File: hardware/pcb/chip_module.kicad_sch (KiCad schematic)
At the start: 200 parts, among them J12 BTB_DAUGHTER

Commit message: pcb: Ironwood SBT socket + per-datasheet pin fixes + no_connect markers
Step 0 — Ironwood SBT open-top spring-pin socket (emitter face, main board):
  - socket_footprint(): 65 solder pads (64 EM + EM_ANODE) on F.Cu+F.Paste+F.Mask
    at the 0.30mm die-contact pitch, 4 NPTH M2 mount holes, 25x25mm body +
    courtyard. lib_id "qssc:Ironwood_SBT" + symbol; Uchip swapped from
    QSSC_Chip_EM. This is the commercial made-to-order socket that fits the
    20x20mm / 0.30mm-pitch die (no off-the-shelf socket exists at that pitch).
  - Head-board QSSC_Chip_DET (detector face) unchanged: ACF/pogo on B.Cu.

Step 1 — per-datasheet pin audit + (no_connect) emission (addresses
"practically nothing connected per its datasheet"):
  - FT232RL: net pin 24 -> +3V3 (VCC) and pin 23 -> GND (AGND) -- both required
    supply/ground pads per SSOP-28 that were previously unnetted.
  - ADF4351: REFIN- (pin 19) decoupled to GND via new C37 100nF (single-ended
    CMOS ref, datasheet Fig.51); unused RFOUTB+/- (13,14), RFOUTA- (15), SW (5),
    CE (25) declared no_connect per datasheet (unused RF outputs float).
  - add() now takes nc_pins=...; emit_schematic() emits (no_connect) sexps at
    every documented-unused pin: FT232 modem/crystal/LED (12 pins), ADF4351 (5),
    AD7616 parallel-DB bus + SDI/SDOB in 1-wire HW mode (10/chip x4 = 40 head),
    TLC5947 chip2 OUT16-23 + SOUT (9 main).

Both boards: DRC 0/0/0, ERC 0 errors / 0 warnings. 9 PCB tests green.

Co-Authored-By: Claude Code <noreply@anthropic.com>
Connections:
- no-connect marks 0 -> 40
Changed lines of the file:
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@@
 		)
+	)
+	(no_connect
+		(at 753.4 188.89)
+	)
+	(no_connect
+		(at 753.4 190.16)
+	)
+	(no_connect
+		(at 753.4 191.43)
+	)
+	(no_connect
+		(at 753.4 192.7)
+	)
+	(no_connect
+		(at 753.4 193.97)
+	)
+	(no_connect
+		(at 753.4 195.24)
+	)
+	(no_connect
+		(at 753.4 196.51)
+	)
+	(no_connect
+		(at 753.4 197.78)
+	)
+	(no_connect
+		(at 753.4 169.84)
+	)
+	(no_connect
+		(at 753.4 168.57)
+	)
+	(no_connect
+		(at 511.4 208.89)
+	)
+	(no_connect
+		(at 511.4 210.16)
+	)
+	(no_connect
+		(at 511.4 211.43)
+	)
+	(no_connect
+		(at 511.4 212.7)
+	)
+	(no_connect
+		(at 511.4 213.97)
+	)
+	(no_connect
+		(at 511.4 215.24)
+	)
+	(no_connect
+		(at 511.4 216.51)
+	)
+	(no_connect
+		(at 511.4 217.78)
+	)
+	(no_connect
+		(at 511.4 189.84)
+	)
+	(no_connect
+		(at 511.4 188.57)
+	)
+	(no_connect
+		(at 687.4 208.89)
+	)
+	(no_connect
+		(at 687.4 210.16)
+	)
+	(no_connect
+		(at 687.4 211.43)
+	)
+	(no_connect
+		(at 687.4 212.7)
+	)
+	(no_connect
+		(at 687.4 213.97)
+	)
+	(no_connect
+		(at 687.4 215.24)
+	)
+	(no_connect
+		(at 687.4 216.51)
+	)
+	(no_connect
+		(at 687.4 217.78)
+	)
+	(no_connect
+		(at 687.4 189.84)
+	)
+	(no_connect
+		(at 687.4 188.57)
+	)
+	(no_connect
+		(at 445.4 228.89)
+	)
+	(no_connect
+		(at 445.4 230.16)
+	)
+	(no_connect
+		(at 445.4 231.43)
+	)
+	(no_connect
+		(at 445.4 232.7)
+	)
+	(no_connect
+		(at 445.4 233.97)
+	)
+	(no_connect
+		(at 445.4 235.24)
+	)
+	(no_connect
+		(at 445.4 236.51)
+	)
+	(no_connect
+		(at 445.4 237.78)
+	)
+	(no_connect
+		(at 445.4 209.84)
+	)
+	(no_connect
+		(at 445.4 208.57)
 	)
 	(sheet_instances

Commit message: pcb: verify netlist complete per datasheets, fix C_in/C37 placement short
Connection audit (tools/audit_connections.py) confirms both boards are
netlist-complete and datasheet-correct BEFORE routing:

  - ERC: 0 errors both boards (qssc + chip_module). The 145/203 remaining
    messages are all endpoint_off_grid warnings (authored symbols on a
    non-1.27 mm pin grid) -- cosmetic noise.
  - DRC: 0 violations, 0 unconnected pads, 0 footprint errors both boards.
  - Chip die: 64 emitter_cat -> TLC5947 OUT sinks + EM_ANODE -> +12V_EMIT
    on the main board; 64 DET_IN -> TLV9004 TIA -> AD7616 + DET_REF on the
    head. Every chip net has an off-chip destination (audit confirms).
  - All 268 main-board + head "unnetted" IC pins are intentional spares,
    not missing connections: FPGA 185 spare IO balls (99 power balls all
    netted), AD7616 parallel-DB bus + SDI/SDOB in 1-wire HW serial mode,
    FT232 modem/CBUS pins (USB-only; pin 23 AGND + 24 VCC ARE netted),
    ADF4351 NC pins 5/13/14/15/25 per datasheet, TLC5947 chip2 unused
    OUT16-23 + SOUT, and numberless EP/mount-hole cosmetic pads.

Fix: the main board had 3 DRC violations (shorting_items +5V_IN/ADF_TEMP,
courtyards_overlap, solder_mask_bridge) all from ONE root cause -- the new
input-bulk cap C_in and the ADF4351 TEMP decoupler C37 both fell through
assign_pcb_positions()'s else-branch to the (50,50) default cell, so
C_in.1 (+5V_IN) overlapped C37.1 (ADF_TEMP). Give both explicit placements
in the fixed dict (C_in @46,8 near the barrel jack; C37 @104,36 below U3).
Regenerated both boards -> DRC 0/0/0.

route_signals.py: the chip-net force-fail referenced an undefined
`structured_chip` (NameError if run). Define it as an empty set so the
file is runnable and all chip nets are cleanly deferred to the future
_structured_bus_fanout (task #36) / FreeRouting -- routing stays paused
per the user's instruction until the netlist was verified.

Adds tools/audit_connections.py (per-datasheet pin/rail/chip audit) a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
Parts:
- added C_5V: 10uF, Capacitor_SMD:C_0805_2012Metric, symbol qssc:C
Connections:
- net +5V: now also C_5V.1
- net GND: now also C_5V.2
- no-connect marks 40 -> 43
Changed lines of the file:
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@@
 	)
 	(symbol
+		(lib_id "qssc:C")
+		(at 0 0 0)
+		(unit 1)
+		(exclude_from_sim no)
+		(in_bom yes)
+		(on_board yes)
+		(dnp no)
+		(property "Reference" "C_5V"
+			(at 0 -2 0)
+			(effects
+				(font
+					(size 1.27 1.27)
+				)
+			)
+		)
+		(property "Value" "10uF"
+			(at 0 2 0)
+			(effects
+				(font
+					(size 1.27 1.27)
+				)
+			)
+		)
+		(property "Footprint" "Capacitor_SMD:C_0805_2012Metric"
+			(at 0 0 0)
+			(effects
+				(font
+					(size 1.27 1.27)
+				)
+				(hide yes)
+			)
+		)
+		(pin "1"
+		)
+		(pin "2"
+		)
+		(instances
+			(project "chip_module"
+				(path "/00000000-0000-0000-0000-000000000001"
+					(reference "C_5V")
+					(unit 1)
+				)
+			)
+		)
+	)
+	(symbol
 		(lib_id "qssc:L")
 		(at 662.0 180.0 0)
@@
 	(symbol
 		(lib_id "power:PWR_FLAG")
+		(at 38 12 0)
+		(unit 1)
+		(exclude_from_sim no)
+		(in_bom no)
+		(on_board no)
+		(dnp no)
+		(property "Reference" "#FLG12"
+			(at 38 10.73 0)
+			(effects
+				(font
+					(size 1.27 1.27)
+				)
+			)
+		)
+		(property "Value" "PWR_FLAG"
+			(at 38 13.27 0)
+			(effects
+				(font
+					(size 1.27 1.27)
+				)
+			)
+		)
+		(property "Footprint" ""
+			(at 38 12 0)
+			(effects
+				(font
+					(size 1.27 1.27)
+				)
+				(hide yes)
+			)
+		)
+		(pin "1"
+		)
+		(instances
+			(project "chip_module"
+				(path "/00000000-0000-0000-0000-000000000001"
+					(reference "#FLG12")
+					(unit 1)
+				)
+			)
+		)
+	)
+	(symbol
+		(lib_id "power:PWR_FLAG")
 		(at 80 132 0)
 		(unit 1)
@@
 	)
 	(label "+5V"
+		(at 0.0 -3.81 0)
+		(fields_autoplaced yes)
+		(effects
+			(font
+				(size 1.27 1.27)
+			)
+			(justify left bottom)
+		)
+	)
+	(label "GND"
+		(at 0.0 3.81 0)
+		(fields_autoplaced yes)
+		(effects
+			(font
+				(size 1.27 1.27)
+			)
+			(justify left bottom)
+		)
+	)
+	(label "+5V"
 		(at 662.0 176.19 0)
 		(fields_autoplaced yes)
@@
 		)
 	)
+	(label "GND"
+		(at 38.0 12.0 0)
+		(fields_autoplaced yes)
+		(effects
+			(font
+				(size 1.27 1.27)
+			)
+			(justify left bottom)
+		)
+	)
 	(label "+5V_A"
 		(at 80.0 132.0 0)
@@
 	)
 	(no_connect
+		(at 511.4 183.49)
+	)
+	(no_connect
 		(at 687.4 208.89)
 	)
@@
 	)
 	(no_connect
+		(at 687.4 183.49)
+	)
+	(no_connect
 		(at 445.4 228.89)
 	)
@@
 		(at 445.4 208.57)
 	)
+	(no_connect
+		(at 445.4 203.49)
+	)
 	(sheet_instances

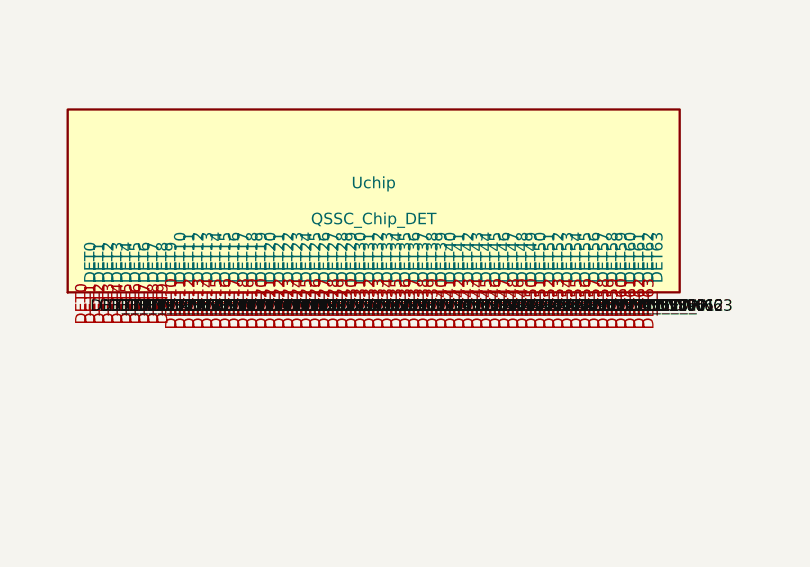
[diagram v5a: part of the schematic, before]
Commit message: fix(detector): add DET_COMMON pad -> DET_REF, close the detector common electrode
The die TOP (detector) face had only 64 DET pixel pads -- the continuous
ITO common back-electrode (DET_COMMON, the shared detector masa per
FABRICATION_PROTOCOL_P0.md: 130 contacts = 64 DET + 64 EM-cathode + 2
ITO commons) was never contacted.  The TIA reference (DET_REF, 1.65 V
virtual ground) existed but had no bond point to the die ITO, so the
photodetector circuit was open on the bias/return side for all 64
graphene/MoS2 pixels.  The emitter face got its common (EM_ANODE); the
detector face did not -- that asymmetry is the defect.

Fix: add a DET_COMMON edge pad to chip_footprint_det() (B.Cu + B.Mask,
mirrors EM_ANODE on the emitter face) and map DET_COMMON -> DET_REF in
chip_net_map_det() + a DET_COMMON pin in chip_pin_list_det().  Zero-bias
short-circuit photocurrent readout (pads held at virtual ground, ITO at
the same 1.65 V -> ~0 V across the photodetector, max responsivity for
the photogating graphene/MoS2 detector; DET_REF only sets the DC
voltage, no net photocurrent flows through it).

route_signals dog-bones the new pad (65 detector-face fanout vias, was
64).  Also corrects stale '0.30 mm pitch' comments -> 2.5 mm (the die
is an 8x8 grid at 2.5 mm, 17.5 mm span on the 20 mm body; 1.2 mm pads
cannot exist at 0.30 mm pitch) and the '4-layer head' -> 6-layer note.
Main board unchanged (detector face is head-only).  ruff CI clean.

Co-Authored-By: Claude Code <noreply@anthropic.com>
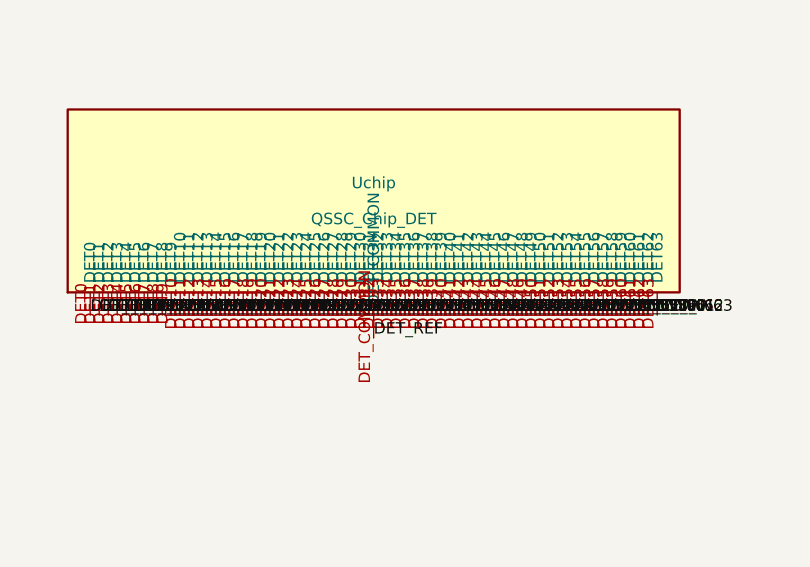
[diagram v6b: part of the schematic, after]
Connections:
- net DET_REF: now also Uchip.DET_COMMON
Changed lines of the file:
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@@
 		(pin "DET63"
 		)
+		(pin "DET_COMMON"
+		)
 		(instances
 			(project "chip_module"
@@
 		(fields_autoplaced yes)
 		(effects
+			(font
+				(size 1.27 1.27)
+			)
+			(justify left bottom)
+		)
+	)
+	(label "DET_REF"
+		(at 80.0 70.24 0)
+		(fields_autoplaced yes)
+		(effects
